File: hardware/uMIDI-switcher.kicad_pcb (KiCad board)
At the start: 2 copper layers, 127 x 50 mm, 107 parts, among them Q1 BSS138, Q2 BSS138, Q3 BSS138, Q4 BSS138, Q5 BSS138, Q6 BSS138, Q7 BSS138, Q8 BSS138, U1 MC7809CD, U2 MC7809CD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

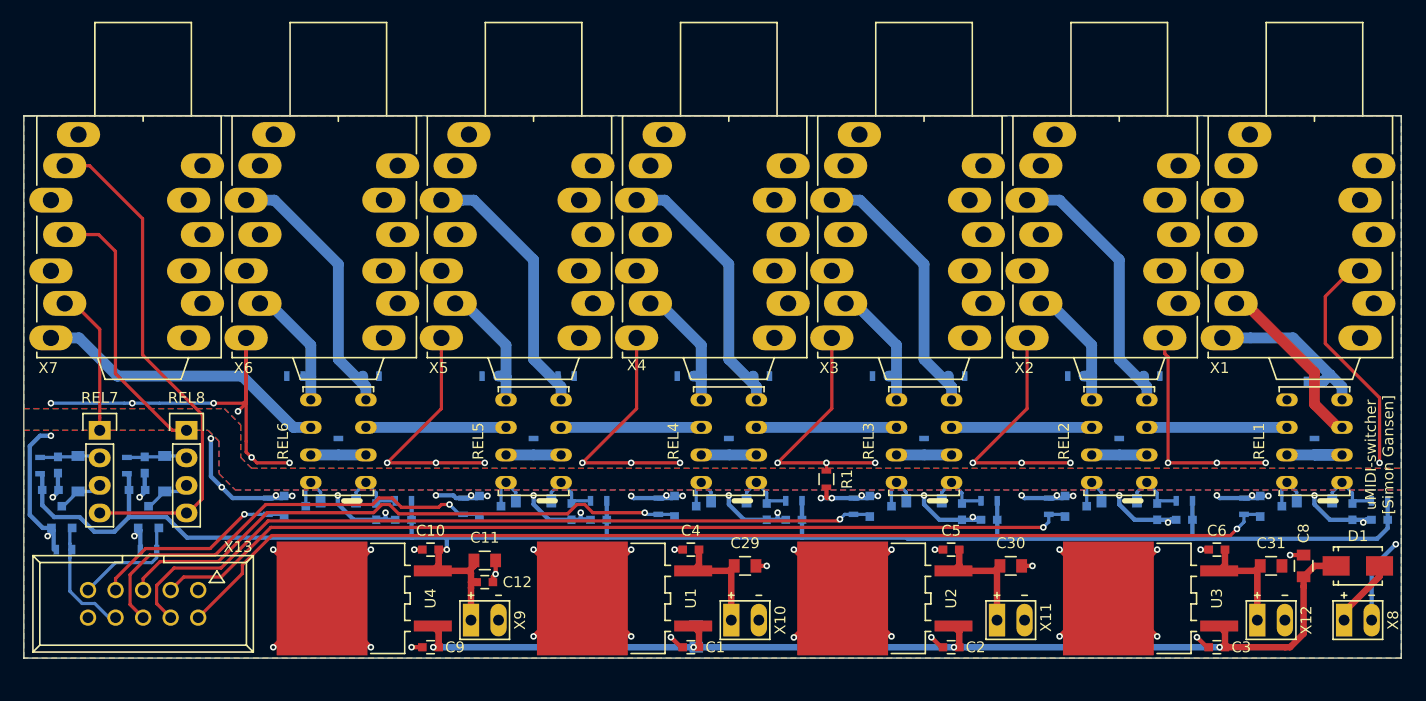
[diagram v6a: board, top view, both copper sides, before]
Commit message: Fix major footprint fuckups...
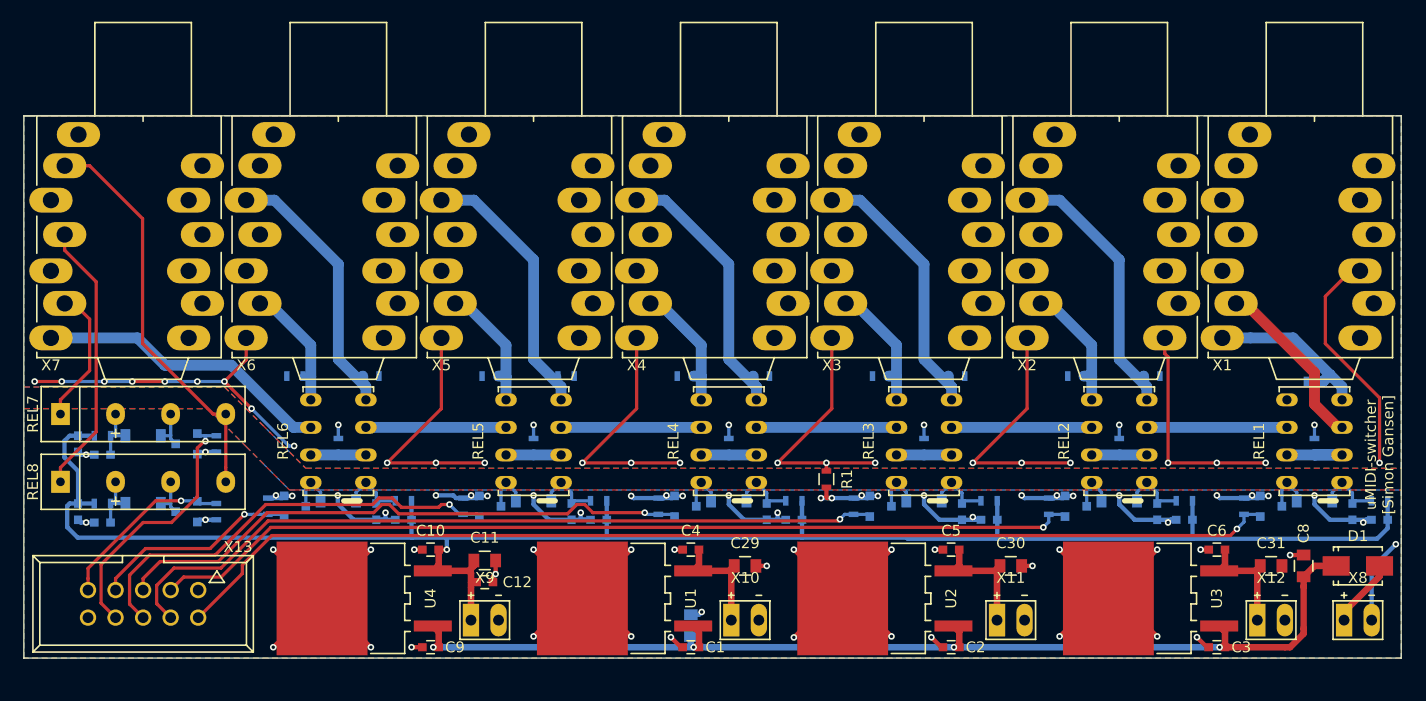
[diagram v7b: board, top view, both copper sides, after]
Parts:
- REL7, REL8: footprint Socket_Strips:Socket_Strip_Straight_1x04 -> uMIDI-switcher:Meder_SIL
- moved R33 17.1 mm to (95.2, 109.2), turned to 270 degrees
- moved Q7 13.3 mm to (92.5, 109.2), turned to 270 degrees
- moved R35 7.16 mm to (95.2, 115.5), turned to 270 degrees
- moved D8 6.95 mm to (88.5, 108.5), turned to 0 degrees
- moved C28 6.58 mm to (84.8, 116.5), turned to 180 degrees
- moved R32 6.37 mm to (84.8, 108.5), turned to 180 degrees
- moved REL8 6.21 mm to (88.5, 112.8), turned to 0 degrees
- moved C27 5.81 mm to (82.5, 115.5), turned to 270 degrees
- moved C25 4.96 mm to (82.5, 109.2), turned to 270 degrees
- moved REL7 4.27 mm to (88.5, 106.5), turned to 0 degrees
- moved C26 4.21 mm to (84.8, 110.2), turned to 180 degrees
- moved R34 4.16 mm to (84.8, 114.8), turned to 180 degrees
- moved Q8 3.54 mm to (92.5, 115.5), turned to 270 degrees
- moved D9 3.40 mm to (88.5, 114.8), turned to 0 degrees
- moved C7 1.12 mm to (139.0, 126.0)
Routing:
- net GND: track 233.0 -> 209.3 mm, vias 66 -> 64
- net /Switch1/Ctrl: track 11.1 -> 25.4 mm, vias 0 -> 1
- net /Switch1/B: track 47.3 -> 37.3 mm
- net GNDA: track 179.2 -> 172.1 mm, vias 22 -> 31
- net /Switch2/Ctrl: track 10.4 -> 16.5 mm, vias 0 -> 1
- net +9V: track 167.4 -> 169.8 mm
- net +12V: track 100.2 -> 101.3 mm
- net /Switch1/A: track 13.5 -> 12.8 mm
- net /Switch1/relais_p: track 5.63 -> 5.12 mm
- net /Switch2/relais_p: track 5.63 -> 5.13 mm

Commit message: Revise silkscreen
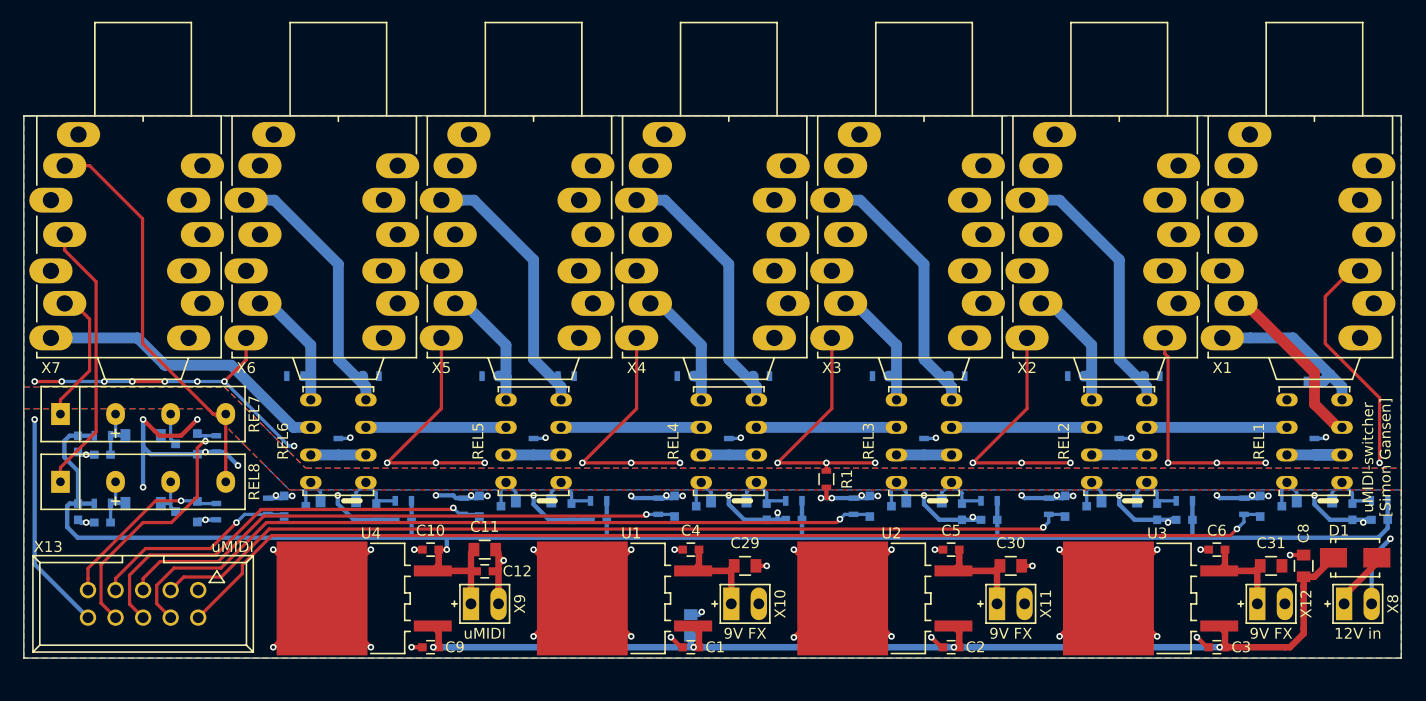
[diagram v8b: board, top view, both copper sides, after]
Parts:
- moved X10 1.50 mm to (144.0, 124.0)
- moved X11 1.50 mm to (168.5, 124.0)
- moved X12 1.50 mm to (192.5, 124.0)
- moved X8 1.50 mm to (200.5, 124.0)
- moved X9 1.50 mm to (120.0, 124.0)
- moved C11 1.00 mm to (120.0, 119.0)
- moved C12 1.00 mm to (120.0, 121.0)
- moved D1 0.79 mm to (200.2, 119.8)
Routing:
- net GND: track 209.3 -> 255.7 mm, vias 64 -> 67
- net Net-(C31-Pad1): track 11.3 -> 9.77 mm
- net Net-(C30-Pad1): track 11.8 -> 10.3 mm
- net Net-(C29-Pad1): track 11.3 -> 9.77 mm
- net /Looper3/Ctrl: track 54.1 -> 52.6 mm
- net /Looper4/Ctrl: track 40.6 -> 39.6 mm
- net /pwr_in: track 6.70 -> 5.85 mm
- net GNDA: track 172.1 -> 171.5 mm, vias 31 -> 30
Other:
- board text added: "12V in"
- board text added: "9V FX"
- board text added: "uMIDI"
